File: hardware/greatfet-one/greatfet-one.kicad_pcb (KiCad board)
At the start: 4 copper layers, 70.6 x 53.3 mm, 103 parts, among them J1 NEIGHBOR1, J2 NEIGHBOR2, J3 USB-MICRO-B-SHIELDED, J4 USB-MICRO-B-SHIELDED, J5 JTAG, J6 POWER, J7 BONUS_ROW, SW1 DFU, SW2 RESET, U1 LPC4330FBD144, U2 W25Q16DV, U3 AP7333, U4 IP4220CZ6, U5 AP2553W6-7, X1 MCU_XTAL, X2 RTC_XTAL

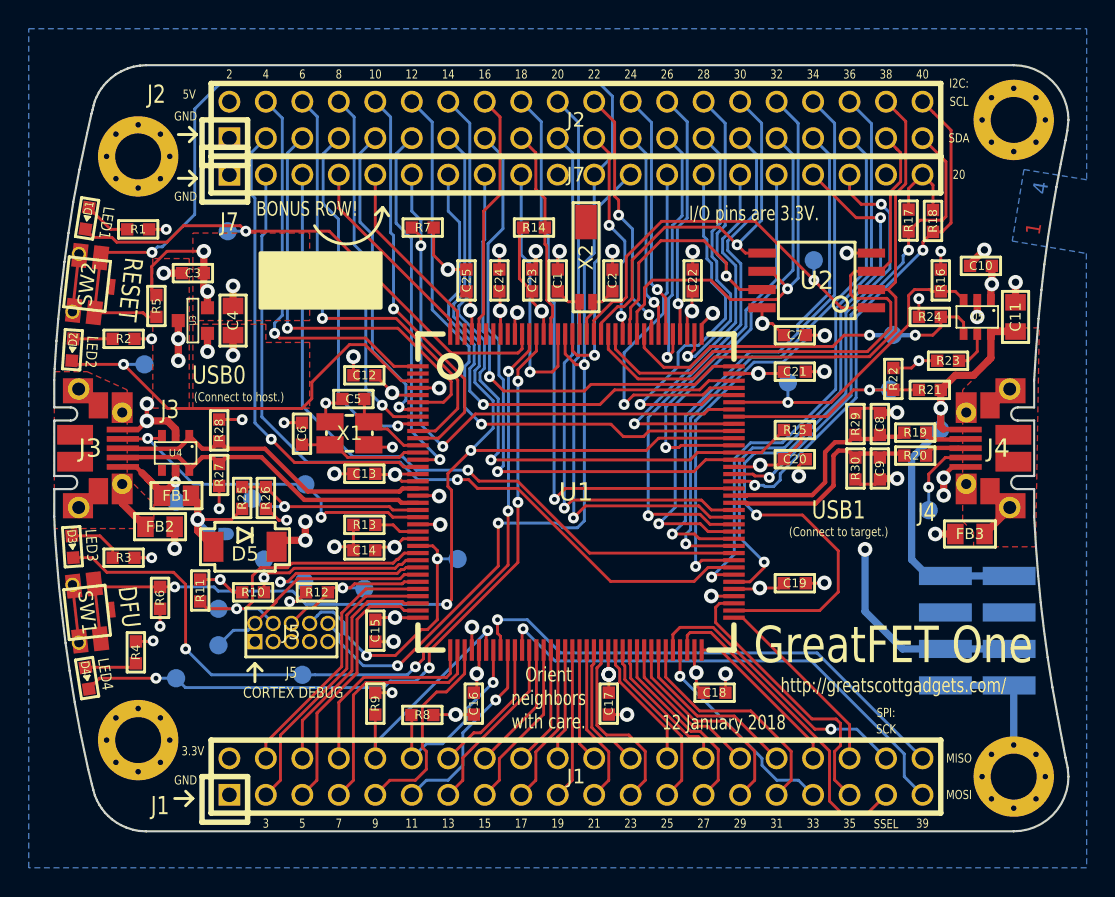
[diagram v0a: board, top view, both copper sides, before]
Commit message: GreatFET One: adjusted component positions to ease hand-assembly
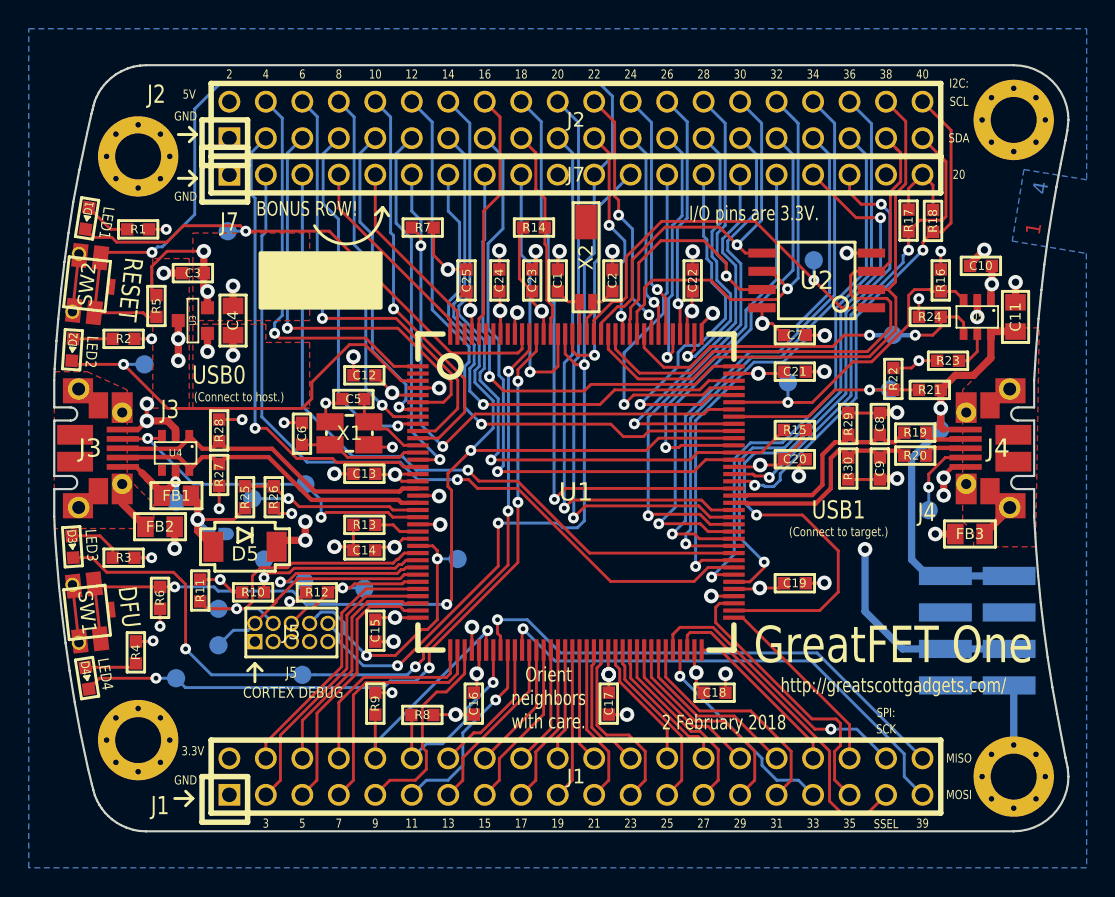
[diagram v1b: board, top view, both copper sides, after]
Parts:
- moved R26 0.55 mm to (121.2, 101.2)
- moved R29 0.50 mm to (161.2, 96.1)
- moved R30 0.50 mm to (161.2, 99.2)
- moved R25 0.21 mm to (119.2, 101.2)
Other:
- board text added: "2 February 2018"
- board text removed: "12 January 2018"
